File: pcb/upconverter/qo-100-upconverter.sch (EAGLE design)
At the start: 171 parts, among them CON1 2EDG-2P, Q1 AO3400, Q2 AO3401, U1 EFM32PG1B200F256GM32, U10 MIC23155, U11 LT8636, U12 ADP3334, U13 LT8636, U14 ADP150UJZ-3.3, U15 ADP150UJZ-3.3, U2 DSB321SDA, U3 ADF4351, U4 F1951NBGI, U5 MAX2671, U6 2450BP15E0100, U7 ADL5601, U8 ADL5601, U9 ADPA9002

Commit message: Start upconverter redesign
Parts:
- removed C82: 10pF, Capacitor:CAPACITOR-0603
- removed C83, C84, C86, C87: 1uF, Capacitor:CAPACITOR-0603
- removed C85, C88: 22uF, Capacitor:CAPACITOR-1206
- removed C89: 100nF, Capacitor:CAPACITOR-0603
- removed C90: 10uF, Capacitor:CAPACITOR-1206
- removed L11: 47nH, Inductor:INDUCTOR-0603
- removed L12: 2.2uH, Inductor:INDUCTOR-2.5X2X1.2MM
- removed L13, L14: 4.7uH, Inductor:INDUCTOR-6X6MM
- removed Q1: AO3400, Alpha Omega:AO3400
- removed Q2: AO3401, Alpha Omega:AO3401
- removed R36: 1M Ohms, Resistor:RESISTOR-0603
- removed R37: 86.6K Ohms, Resistor:RESISTOR-0603
- removed TP1: TESTPOINT-1.27MM, PADs:TESTPOINT-1.27MM
- C11, C13, C15, C17: value 100nF -> 10pF
- C12, C14, C16, C67: value 10pF -> 100nF
- C18: value 10pF -> 0.7pF
- C20: value 0.7pF -> 15pF
- C21: value 15pF -> 39nF
- C22: value 39nF -> 2.7nF
- C23: value 2.7nF -> 1.2nF
- C24: value 1.2nF -> 100nF
- C26, C28: value 10uF -> 100nF
- C27: value 100nF -> 10uF
- C29: value 100nF -> 100pF
- C30: value 100pF -> 47pF
- C32: value 47pF -> 220pF
- C33: value 220pF -> 15pF
- C34, C49: value DNP -> 100uF; device Capacitor:CAPACITOR-0603 -> Capacitor:CAPACITOR-1206
- C35, C39, C50: value 15pF -> 1uF
- C36: value 100uF -> 1nF; device Capacitor:CAPACITOR-1206 -> Capacitor:CAPACITOR-0603
- C37, C41: value 1uF -> 15pF
- C38, C42: value 1nF -> 15pF
- C4: value 4.7uF -> 1uF
- C40: value 15pF -> 1nF
- C43: value 15pF -> 100nF
- C45: value 0 Ohms -> 10uF
- C46: value 12pF -> 10nF
- C47: value 22uF -> 100pF; device Capacitor:CAPACITOR-1206 -> Capacitor:CAPACITOR-0603; VOLTAGE 25V -> (none)
- C48: value 1nF -> 2pF
- C5, C72: value 1uF -> 100nF
- C51: value DNP -> 3.3F
- C52: value DNP -> 100nF
- C53: value DNP -> 10nF
- C54: value 1nF -> 100pF
- C55: value 100nF -> 15pF
- C56: value 4.7uF -> 15pF; VOLTAGE 35V -> (none)
- C57: VOLTAGE (none) -> 35V
- C58: value 470pF -> 100nF
- C60: value 470pF -> 4.7uF
- C61: value 1uF -> 470pF; VOLTAGE 50V -> (none)
- C62: VOLTAGE (none) -> 50V
- C63, C80: value 10nF -> 470pF
- C64, C78: value 470pF -> 1uF
- C65: value 100nF -> 10nF
- C66: value 100nF -> 470pF
- C68: value 470pF -> 10pF
- C69: value 100uF -> 100nF; device Capacitor:CAPACITOR-1206 -> Capacitor:CAPACITOR-0603
- C71: value 100nF -> 100uF; device Capacitor:CAPACITOR-0603 -> Capacitor:CAPACITOR-1206
- C73: value 4.7uF -> 1uF; VOLTAGE 35V -> (none)
- C74: value 22uF -> 470pF; device Capacitor:CAPACITOR-1206 -> Capacitor:CAPACITOR-0603; VOLTAGE 25V -> (none)
- C75, C77: VOLTAGE 50V -> (none)
- C76: value 100nF -> 1uF
- C81: value 100nF -> 10uF; device Capacitor:CAPACITOR-0603 -> Capacitor:CAPACITOR-1206; VOLTAGE (none) -> 50V
- L1: value 4.7uH -> 3.3nH; OCLCSC C281111 -> (none)
- L10: value 470nH -> 4.7uH; device Inductor:INDUCTOR-0603 -> Inductor:INDUCTOR-6X6MM; CURRENT (none) -> 3A; OCLCSC (none) -> C326336
- L2: value 3.3nH -> 10nH
- L3: value 10nH -> 3.3nH
- L5: value 3.3nH -> 1.8nH
- L6: value 1.8nH -> 470nH
- L7: value DNP -> 470nH
- L8: value DNP -> 47nH
- L9: value 470nH -> 2.2uH; device Inductor:INDUCTOR-0603 -> Inductor:INDUCTOR-2.5X2X1.2MM; CURRENT (none) -> 2.2A; OCLCSC (none) -> C375952
- R10: value 100K Ohms -> 61.9 Ohms
- R11: value 100 Ohms -> 680 Ohms
- R12: value 100K Ohms -> 105 Ohms
- R13: value 510 Ohms -> 100K Ohms
- R14: value 2K Ohms -> 100 Ohms
- R15, R17: value 147K Ohms -> 100K Ohms
- R16: value 21K Ohms -> 510 Ohms
- R18: value 21K Ohms -> 100 Ohms
- R19: value 41.2K Ohms -> 510 Ohms
- R20: value 309K Ohms -> 147K Ohms
- R21: value 71.5K Ohms -> 21K Ohms
- R22: value 100K Ohms -> 41.2K Ohms
- R24: value 1M Ohms -> 100K Ohms
- R25: value 226K Ohms -> 309K Ohms
- R26: value 22 Ohms -> 71.5K Ohms
- R27: value 510 Ohms -> 1M Ohms
- R28: value 10K Ohms -> 226K Ohms
- R29: value 10K Ohms -> 510 Ohms
- R30: value 3.9K Ohms -> 100K Ohms
- R31: value 100K Ohms -> 210K Ohms
- R32: value 210K Ohms -> 64.9K Ohms
- R33: value 64.9K Ohms -> 100K Ohms
- R34: value 41.2K Ohms -> 210K Ohms
- R35: value 100K Ohms -> 64.9K Ohms
- R8: value 360 Ohms -> 105 Ohms
- R9: value 680 Ohms -> 360 Ohms
- U1: value EFM32PG1B200F256GM32 -> EFM32PG1B100F256GM32; device EFM32:EFM32PG1B200F256GM32 -> EFM32:EFM32PG1B100F256GM32
- U13: value LT8636 -> ADP7142AUJZ-3.3; device Analog Devices:LT8636 -> Analog Devices:ADP7142AUJZ-3.3
- U14: value ADP150UJZ-3.3 -> ADP7142AUJZ-3.3; device Analog Devices:ADP150UJZ-3.3 -> Analog Devices:ADP7142AUJZ-3.3
- U15: value ADP150UJZ-3.3 -> ADP3334; device Analog Devices:ADP150UJZ-3.3 -> Analog Devices:ADP3334
- U2: value DSB321SDA -> ADF4351; device Crystal:DSB321SDA -> Analog Devices:ADF4351
- U3: value ADF4351 -> F1951NBGI; device Analog Devices:ADF4351 -> Renesas:F1951NBGI
- U4: value F1951NBGI -> MAX2671; device Renesas:F1951NBGI -> Maxim Integrated:MAX2671
- U5: value MAX2671 -> 2450BP15E0100; device Maxim Integrated:MAX2671 -> Generic Filter:2450BP15E0100
- U6: value 2450BP15E0100 -> ADL5601; device Generic Filter:2450BP15E0100 -> Analog Devices:ADL5601
- U8: value ADL5601 -> F1951NBGI; device Analog Devices:ADL5601 -> Renesas:F1951NBGI
- U9: value ADPA9002 -> ADL5606; device Analog Devices:ADPA9002 -> Analog Devices:ADL5606
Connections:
- removed net !5V0_PA_BIAS_EN: R31.1, U1.PA0, U12.SD
- removed net !ATT_CS: R10.2, U1.PB15, U4.!CS
- removed net 12V0: C82.C1, C85.C1, C88.C1, C89.C1, L14.2, Q2.S, R17.2, R29.2, R36.2, U13.BIAS
- removed net 12V0_ANA_PA_CLEAN: C46.C1, C47.C1, C74.C1, C76.C1, L11.2, Q2.D, R14.2
- removed net 12V0_BST: C81.C2, U13.BST
- removed net 12V0_FB: C82.C2, R36.1, R37.2, U13.FB
- removed net 12V0_INTVCC: C79.C1, U13.INTVCC, U13.SYNC/MODE
- removed net 12V0_PA_BIAS_EN: R26.2, U1.PA1
- removed net 12V0_PGOOD: R35.1, U1.PB14, U13.PG
- removed net 12V0_RT: R34.2, U13.RT
- removed net 12V0_SS: C80.C1, U13.TR/SS
- removed net 12V0_SW: C81.C1, L14.1, U13.SW
- removed net 12V0_VSENSE: C64.C1, R17.1, R18.2, U1.PB12
- removed net 1V8: C4.C1, L1.1, U1.DVDD
- removed net 3V3_ANA_MIXER_CLEAN: C26.C1, C28.C1, C29.C1, C31.C1, C32.C1, C86.C1, L6.2, U14.OUT, U4.VDD, U5.VCC
- removed net 5V0_ANA_PA_CLEAN: C36.C1, C37.C1, C38.C1, C39.C1, C41.C1, C42.C1, C43.C1, C78.C1, L10.2, L9.2, R13.2, R32.2, U12.OUT
- removed net N$11: C45.C1, TP1.TP, U9.VGG
- removed net N$13: C50.C1, L11.1, U9.RFOUT
- removed net N$17: C44.C2, U9.RFIN
- removed net N$21: L1.2, U1.VREGSW
- removed net N$24: D3.A, R14.1
- new net !IF_ATT_CS: U1.PB15, U3.!CS
- new net !IF_ATT_RST: R13.2, U3.!RST
- new net !PA_BIAS_EN: R30.1, R33.1, U1.PA0, U12.SD, U15.SD
- new net !RF_ATT_CS: U8.!CS
- new net !RF_ATT_RST: R17.2, U8.!RST
- new net 3V3_ANA_MIXER_ATT_CLEAN: C25.C1, C27.C1, C28.C1, C30.C1, C31.C1, C43.C1, C78.C1, L5.2, U13.SENSE/ADJ, U13.VOUT, U3.VDD, U4.VCC, U8.VDD
- new net 5V0_PA_STG1_CLEAN: C34.C1, C35.C1, C36.C1, C37.C1, C39.C1, C40.C1, C41.C1, C74.C1, L6.2, L7.2, R16.2, R31.2, U12.OUT
- new net 5V0_PA_STG2_CLEAN: C45.C1, C46.C1, C47.C1, C49.C1, C50.C1, C53.C1, C54.C1, C55.C1, C80.C1, L8.2, R19.2, R34.2, U15.OUT, U9.VBIAS, U9.VCC
- new net N$29: C20.C2, R10.2, R8.2
- new net PA_DISABLE: R18.1
- new net RF_ACC_PRE: C42.C2, U8.RF2
- net !MIXER_SHDN: now also R14.2; no longer R11.2
- net !PLL_MUTE: now also U2.!PDRF; no longer U3.!PDRF
- net 3V3: now also C10.C1, C70.C1, L9.2, R25.2, R30.2, R33.2, U1.DVDD, U2.DVDD; no longer C11.C1, C65.C1, L12.2, R20.2, R31.2, R35.2, U1.VREGVDD, U3.DVDD
- net 3V3_ANA_PLL_CLEAN: now also C6.C1, C79.C1, L1.1, L2.2, U14.SENSE/ADJ, U14.VOUT, U2.AVDD, U2.SDVDD, U2.VP, U2.VVCO@0, U2.VVCO@1; no longer C10.C1, C87.C1, L2.1, L3.2, U15.OUT, U2.VDD, U3.AVDD, U3.SDVDD, U3.VP, U3.VVCO@0, U3.VVCO@1
- net 3V3_FB: now also R25.1, R26.2; no longer R20.1, R21.2
- net 3V3_SOFTSTART: now also C63.C1; no longer C60.C1
- net 3V3_SW: now also L9.1; no longer L12.1
- net 5V0: now also C58.C1, C60.C1, C68.C1, C73.C1, C75.C1, C76.C1, C77.C1, L10.2, R23.2, R29.2, U13.EN, U13.VIN, U15.IN; no longer C55.C1, C57.C1, C67.C1, C70.C1, C83.C1, C84.C1, L13.2, R22.2, R24.2, U15.EN, U15.VIN
- net 5V0_BST: now also C67.C2; no longer C66.C2
- net 5V0_FB: now also C68.C2, R27.1, R28.2; no longer C67.C2, R24.1, R25.2
- net 5V0_INTVCC: now also C64.C1; no longer C62.C1
- net 5V0_RT: now also R22.2; no longer R19.2
- net 5V0_SS: now also C65.C1; no longer C63.C1
- net 5V0_SW: now also C67.C1, L10.1; no longer C66.C1, L13.1
- net 5V0_VSENSE: now also C66.C1, R23.1, R24.2; no longer C68.C1, R22.1, R23.2
- net GND: now also C12.C2, C19.C2, C22.C2, C25.C2, C27.C2, C35.C2, C40.C2, C50.C2, C66.C2, C78.C2, C81.C2, R13.1, R15.1, R17.1, R22.1, R24.1, R26.1, R32.1, R35.1, R9.1, U2.AGND, U2.AGNDVCO@0, U2.AGNDVCO@1, U2.AGNDVCO@2, U2.CPGND, U2.DGND, U2.SDGND, U6.GND@0, U6.GND@1, U8.GND; no longer C11.C2, C18.C2, C20.C2, C24.C2, C26.C2, C32.C2, C38.C2, C42.C2, C56.C2, C68.C2, C74.C2, C80.C2, C83.C2, C84.C2, C85.C2, C86.C2, C87.C2, C88.C2, C89.C2, C90.C2, L7.2, L8.2, Q1.S, R10.1, R16.1, R18.1, R19.1, R23.1, R25.1, R33.1, R34.1, R37.1, U1.VREGVSS, U3.AGND, U3.AGNDVCO@0, U3.AGNDVCO@1, U3.AGNDVCO@2, U3.CPGND, U3.DGND, U3.SDGND, U6.GND, U8.GND@0, U8.GND@1
- net IF_FREQ_SEL: now also C5.C1; no longer C6.C1
- net IF_IN_DCC: now also C24.C1; no longer C25.C1
- net MIXER_LO: now also R10.1, R12.2, U4.LO; no longer C21.C2, U5.LO
- net N$1: now also C18.C2, C20.C1, L3.1; no longer C19.C2, C21.C1, L4.1
- net N$10: now also C52.C1, R18.2, U9.DISABLE; no longer C54.C1, U9.ACG1
- net N$12: now also C33.C2, U6.RFIN; no longer C35.C2, U7.RFIN
- net N$14: now also C38.C1, L6.1, U6.RFOUT; no longer C40.C1, L9.1, U7.RFOUT
- net N$149: now also R29.1; no longer R27.1
- net N$15: now also C38.C2, U7.RFIN; no longer C40.C2, U8.RFIN
- net N$16: now also C42.C1, L7.1, U7.RFOUT; no longer C44.C1, L10.1, U8.RFOUT
- net N$18: now also C56.C2; no longer C50.C2
- net N$2: now also C80.C2, R34.1, R35.2, U15.FB; no longer Q1.G, R26.1, R28.2
- net N$20: now also C74.C2, R31.1, R32.2; no longer C78.C2, R32.1, R33.2
- net N$22: now also C4.C1; no longer C5.C1
- net N$23: now also R16.1; no longer R13.1
- net N$26: now also C24.C2, U3.RF2; no longer C25.C2, U4.RF2
- net N$27: now also C26.C2, U4.IFIN; no longer C27.C2, U5.IFIN
- net N$28: now also C26.C1, U3.RF1; no longer C27.C1, U4.RF1
- net N$3: now also D3.A, R19.1; no longer Q2.G, R29.1, R30.2
- net N$4: now also C29.C1, R14.1, R15.2, U4.!SHDN; no longer C30.C1, R11.1, R12.2, U5.!SHDN
- net N$5: now also C44.C2, C48.C1, U9.RFIN; no longer Q1.D, R30.1
- net N$6: now also C32.C1, L4.2, L5.1; no longer C33.C1, L5.2, L6.1
- net N$67: now also C19.C1, L2.1, L3.2, U2.RFOUTA-; no longer C20.C1, L3.1, L4.2, U3.RFOUTA-
- net N$69: now also C18.C1, L1.2, U2.RFOUTA+; no longer C19.C1, L2.2, U3.RFOUTA+
- net N$7: now also L4.1, U4.RFOUT; no longer L5.1, U5.RFOUT
- net N$8: now also C56.C1, L8.1, U9.RFOUT; no longer C48.C1, C49.C1, U9.ACG3
- net N$84: now also C21.C2, R9.2; no longer C22.C2, R8.2
- net N$88: now also U2.RSET; no longer U3.RSET
- net N$9: now also C44.C1, U8.RF1; no longer C52.C1, C53.C1, U9.ACG2
- net PLL_CP_VOUT: now also C21.C1, R11.2, U2.CPOUT; no longer C23.C1, R9.2, U3.CPOUT
- net PLL_EN: now also U2.CE; no longer U3.CE
- net PLL_FASTLOCK_SW: now also U2.SW; no longer U3.SW
- net PLL_LE: now also U2.LE; no longer U3.LE
- net PLL_LOCK: now also U2.LD; no longer U3.LD
- net PLL_MUXOUT: now also U2.MUXOUT; no longer U3.MUXOUT
- net PLL_REF_ACC: now also C11.C2, U2.REFIN; no longer C12.C2, U3.REFIN
- net PLL_REF_DCC: now also C11.C1; no longer C12.C1, U2.CLK
- net PLL_TEMP: now also C16.C1, U2.TEMP; no longer C18.C1, U3.TEMP
- net PLL_VCOM: now also C14.C1, U2.VCOM; no longer C16.C1, U3.VCOM
- net PLL_VREF: now also C12.C1, U2.VREF; no longer C14.C1, U3.VREF
- net PLL_VTUNE: now also C23.C1, R11.1, U2.VTUNE; no longer C24.C1, R9.1, U3.VTUNE
- net RF_ACC: now also C32.C2, U5.RFIN; no longer C33.C2, C34.C1, L7.1, U6.RFIN
- net RF_ACC_FILT: now also C33.C1, U5.RFOUT; no longer C35.C1, L8.1, U6.RFOUT
- net SPI_MOSI: now also U2.DATA, U3.SDI, U8.SDI; no longer U3.DATA, U4.SDI
- net SPI_SCK: now also U2.CLK, U8.CLK; no longer U4.CLK
- net VIN: now also C57.C1, C62.C1, C81.C1, R20.2; no longer C56.C1, C61.C1, C73.C1, C75.C1, C77.C1, C90.C1, R15.2, U13.EN/UV, U13.VIN
- net VIN_VSENSE: now also C61.C1, R20.1, R21.2; no longer C58.C1, R15.1, R16.2
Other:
- note added: "+20 dB"
- note added: "-9 dB Pi Attenuator"
- note removed: "+13 dB to +15 dB"
- note removed: "Use 68.1K to get higher output power from the last amplifier stage"
- note removed: "VGSon = -8.7V"
- note removed: "Vout = ((R36/R37) + 1) * 0.97"

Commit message: Work on Upconverter
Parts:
- removed JP1: PINHD-1X3, Pin Header:PINHD-1X3
- added C82: 10uF, Capacitor:CAPACITOR-0603
- added C83: 1nF, Capacitor:CAPACITOR-0603
- added C84: 470pF, Capacitor:CAPACITOR-0603
- added C85: 10uF, Capacitor:CAPACITOR-1206
- added CON2: 2EDG-2P-5MM, Generic Connector:2EDG-2P-5MM
- added D6: LED0603, LED:LED0603
- added R36: 210K Ohms, Resistor:RESISTOR-0603
- added R37: 64.9K Ohms, Resistor:RESISTOR-0603
- added R38: 510 Ohms, Resistor:RESISTOR-0603
- added R39: 330 Ohms, Resistor:RESISTOR-0603
- added U16: ADP7142AUJZ-3.3, Analog Devices:ADP7142AUJZ-3.3
- added U17: ADP3334, Analog Devices:ADP3334
- added U18: ADM7171ACPZ-5.0, Analog Devices:ADM7171ACPZ-5.0
- C10, C12, C14, C16, C67: value 100nF -> 10pF
- C11, C13, C15: value 10pF -> 100nF
- C17: value 10pF -> 0.7pF
- C19: value 0.7pF -> 15pF
- C20: value 15pF -> 39nF
- C21: value 39nF -> 2.7nF
- C22: value 2.7nF -> 1.2nF
- C23: value 1.2nF -> 100nF
- C26: value 100nF -> 1uF
- C27: value 10uF -> 100nF
- C28: value 100nF -> 100pF
- C29: value 100pF -> 47pF
- C31: value 47pF -> 220pF
- C32: value 220pF -> 15pF
- C33: value 15pF -> 100uF; device Capacitor:CAPACITOR-0603 -> Capacitor:CAPACITOR-1206
- C34, C49: value 100uF -> 1uF; device Capacitor:CAPACITOR-1206 -> Capacitor:CAPACITOR-0603
- C35, C39: value 1uF -> 1nF
- C36, C40: value 1nF -> 15pF
- C38: value 15pF -> 1uF
- C42, C56: value 15pF -> 100nF
- C43, C52: value 100nF -> 15pF
- C44: value 15pF -> 10uF
- C45: value 10uF -> 10nF
- C46: value 10nF -> 100uF; device Capacitor:CAPACITOR-0603 -> Capacitor:CAPACITOR-1206
- C50, C64: value 1uF -> 10nF
- C51: value 3.3F -> 100pF
- C53: value 10nF -> 3.3F
- C54: value 100pF -> 15pF
- C55: value 15pF -> 4.7uF; VOLTAGE (none) -> 35V
- C57: value 4.7uF -> 470pF; VOLTAGE 35V -> (none)
- C58: value 100nF -> 470pF
- C59: value 1uF -> 4.7uF; VOLTAGE 50V -> (none)
- C60: value 4.7uF -> 1uF; VOLTAGE (none) -> 50V
- C63: value 470pF -> 1uF
- C65: value 10nF -> 100nF
- C66: value 470pF -> 100nF
- C68: value 10pF -> 1uF
- C73: value 1uF -> 100nF
- C74: value 470pF -> 22uF; device Capacitor:CAPACITOR-0603 -> Capacitor:CAPACITOR-1206
- C75: value 1uF -> 15pF
- C80: value 470pF -> 33nF
- C81: device Capacitor:CAPACITOR-1206 -> Capacitor:CAPACITOR-0603; VOLTAGE 50V -> (none)
- CON1: value 2EDG-2P -> 3P-SH-SIDE; device Generic Connector:2EDG-2P -> JST:3P-SH-SIDE
- D4: value LED0603 -> SMAJ24A; device LED:LED0603 -> TVS:SMAJ24A; COLOR GREEN -> (none)
- D5: value SMAJ24A -> LED0603; device TVS:SMAJ24A -> LED:LED0603; COLOR (none) -> GREEN
- R10: value 61.9 Ohms -> DNP
- R11: value 680 Ohms -> 105 Ohms
- R12: value 105 Ohms -> 360 Ohms
- R13: value 100K Ohms -> 61.9 Ohms
- R14: value 100 Ohms -> 680 Ohms
- R15: value 100K Ohms -> 105 Ohms
- R16: value 510 Ohms -> 100K Ohms
- R17, R4, R5: value 100K Ohms -> 100 Ohms
- R18: value 100 Ohms -> 100K Ohms
- R2: value 10K Ohms -> 1K Ohms
- R20: value 147K Ohms -> 100K Ohms
- R21: value 21K Ohms -> 510 Ohms
- R22: value 41.2K Ohms -> 100K Ohms
- R23: value 100K Ohms -> 10K Ohms
- R25: value 309K Ohms -> 100K Ohms
- R26: value 71.5K Ohms -> 41.2K Ohms
- R27: value 1M Ohms -> 309K Ohms
- R28: value 226K Ohms -> 71.5K Ohms
- R29: value 510 Ohms -> 1M Ohms
- R3: value 330 Ohms -> 1K Ohms
- R30: value 100K Ohms -> 226K Ohms
- R31: value 210K Ohms -> 10K Ohms
- R32: value 64.9K Ohms -> 10K Ohms
- R33: value 100K Ohms -> 0.03 Ohms; device Resistor:RESISTOR-0603 -> Resistor:RESISTOR-1206; TOLERANCE (none) -> 1%
- R34: value 210K Ohms -> 100K Ohms
- R35: value 64.9K Ohms -> 100K Ohms
- R6: value 5.1K Ohms -> 330 Ohms
- R7: value DNP -> 100K Ohms
- R8: value 105 Ohms -> 100K Ohms
- R9: value 360 Ohms -> 5.1K Ohms
- U12: value ADP3334 -> MCP3421-A0; device Analog Devices:ADP3334 -> Microchip:MCP3421-A0
- U13: value ADP7142AUJZ-3.3 -> MCP6C02-020; device Analog Devices:ADP7142AUJZ-3.3 -> Microchip:MCP6C02-020
- U14: value ADP7142AUJZ-3.3 -> TX-8010-EAW-1070-25M0000000; device Analog Devices:ADP7142AUJZ-3.3 -> Microchip:TX-8010-EAW-1070-25M0000000
- U15: value ADP3334 -> ADP7142AUJZ-3.3; device Analog Devices:ADP3334 -> Analog Devices:ADP7142AUJZ-3.3
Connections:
- removed net !PA_BIAS_EN: R30.1, R33.1, U1.PA0, U12.SD, U15.SD
- removed net 3V3_ANA_MIXER_ATT_CLEAN: C25.C1, C27.C1, C28.C1, C30.C1, C31.C1, C43.C1, C78.C1, L5.2, U13.SENSE/ADJ, U13.VOUT, U3.VDD, U4.VCC, U8.VDD
- removed net 3V3_ANA_PLL_CLEAN: C6.C1, C7.C1, C79.C1, C8.C1, C9.C1, L1.1, L2.2, U14.SENSE/ADJ, U14.VOUT, U2.AVDD, U2.SDVDD, U2.VP, U2.VVCO@0, U2.VVCO@1
- removed net IF_FREQ_SEL: C5.C1, JP1-2.S, R2.2, U1.PC11
- removed net PA_DISABLE: R18.1
- removed net PLL_REF_DCC: C11.C1
- new net !PA_STG1_BIAS_EN: R35.1, U1.PB12, U17.SD
- new net 3V3_MIXER_CLEAN: C24.C1, C26.C1, C27.C1, C29.C1, C30.C1, C81.C1, L5.2, U15.SENSE/ADJ, U15.VOUT, U3.VDD, U4.VCC
- new net 3V3_PLL_CLEAN: C5.C1, C6.C1, C7.C1, C8.C1, C82.C1, L1.1, L2.2, U14.OE, U14.VDD, U16.SENSE/ADJ, U16.VOUT, U2.AVDD, U2.SDVDD, U2.VP, U2.VVCO@0, U2.VVCO@1
- new net 5V0_ISENSE: C74.C1, C76.C1, C77.C1, C78.C1, C79.C1, R33.1, U13.VIM, U15.EN, U15.VIN, U16.EN, U16.VIN, U17.IN, U18.VIN
- new net 5V0_ISENSE_VN: C72.C2, R32.1, U12.VIN-
- new net 5V0_ISENSE_VP: C72.C1, R31.1, U12.VIN+
- new net I2C_SCL: R2.1, U1.PC7, U12.SCL
- new net I2C_SDA: R3.1, U1.PC8, U12.SDA
- new net N$11: CON1-2.S, R5.1
- new net N$13: D6.A, R39.1
- new net N$17: CON1-1.S, R4.1
- new net N$21: C10.C1, C75.C1, U14.CLK
- new net N$24: C80.C1, U14.FLT
- new net PA_STG2_BIAS_EN: R34.2, U1.PB13, U18.EN
- new net UART_RX: R4.2, U1.PC10
- new net UART_TX: R5.2, U1.PC11
- net !IF_ATT_CS: now also U1.PF3; no longer U1.PB15
- net !IF_ATT_RST: now also R16.2, U1.PF4; no longer R13.2
- net !MIXER_SHDN: now also R17.2, U1.PD9; no longer R14.2, U1.PF3
- net !PLL_MUTE: now also R8.2, U1.PD15; no longer R5.2, U1.PD14
- net !RF_ATT_CS: now also U1.PA0
- net !RF_ATT_RST: now also R20.2, U1.PA1; no longer R17.2
- net 3V3: now also C65.C1, C9.C1, R2.2, R27.2, R3.2, R35.2, U12.VDD; no longer C10.C1, JP1-1.S, R25.2, R30.2, R33.2
- net 3V3_FB: now also R27.1, R28.2; no longer R25.1, R26.2
- net 3V3_SOFTSTART: now also C61.C1; no longer C63.C1
- net 5V0: now also C56.C1, C59.C1, C67.C1, R24.2, R33.2, R38.2, U13.VDD, U13.VIP; no longer C58.C1, C60.C1, C72.C1, C75.C1, C76.C1, C77.C1, R23.2, R27.2, U12.IN, U13.EN, U13.VIN, U14.EN, U14.VIN, U15.IN
- net 5V0_BST: now also C66.C2; no longer C67.C2
- net 5V0_FB: now also C67.C2, R29.1, R30.2; no longer C68.C2, R27.1, R28.2
- net 5V0_INTVCC: now also C63.C1; no longer C64.C1
- net 5V0_PA_STG1_CLEAN: now also C33.C1, C38.C1, C42.C1, C84.C1, R19.2, R36.2, U17.OUT, U8.VDD; no longer C37.C1, C41.C1, C74.C1, R16.2, R31.2, U12.OUT
- net 5V0_PA_STG2_CLEAN: now also C44.C1, C51.C1, C52.C1, R21.2, U18.SENSE, U18.VOUT; no longer C53.C1, C54.C1, C55.C1, C80.C1, R19.2, R34.2, U15.OUT
- net 5V0_RT: now also R26.2; no longer R22.2
- net 5V0_SS: now also C64.C1; no longer C65.C1
- net 5V0_SW: now also C66.C1; no longer C67.C1
- net 5V0_VSENSE: now also C58.C1, R24.1, R25.2, U1.PB14; no longer C66.C1, R23.1, R24.2, U1.PB11
- net GND: now also C11.C2, C18.C2, C21.C2, C24.C2, C26.C2, C33.C2, C38.C2, C42.C2, C44.C2, C56.C2, C68.C2, C74.C2, C80.C2, C82.C2, C83.C2, C85.C2, CON1-3.S, CON2-1.S, D4.A, D5.C, D6.C, R11.1, R16.1, R18.1, R20.1, R23.1, R25.1, R30.1, R32.2, R34.1, R37.1, R7.1, U12.VSS, U13.VREF, U13.VSS, U16.GND, U17.GND, U18.GND, U9.DISABLE; no longer C10.C2, C17.C2, C19.C2, C23.C2, C25.C2, C31.C2, C37.C2, C41.C2, C43.C2, C54.C2, C66.C2, C72.C2, CON1-1.S, D4.C, D5.A, JP1-3.S, R13.1, R17.1, R2.1, R21.1, R22.1, R24.1, R32.1, R35.1, R4.1, R5.1, R6.1, U12.GND, U13.GND
- net IF_IN_DCC: now also C23.C1; no longer C24.C1
- net LED: now also R6.2, U1.PC9; no longer R3.2, U1.PC10
- net MIXER_LO: now also R13.1, R15.2; no longer R10.1, R12.2
- net N$1: now also C17.C2, C19.C1; no longer C18.C2, C20.C1
- net N$10: now also R31.2, U13.VOUT; no longer C52.C1, R18.2, U9.DISABLE
- net N$12: now also C32.C2; no longer C33.C2
- net N$14: now also C37.C1; no longer C38.C1
- net N$149: now also D5.A, R38.1; no longer D4.A, R29.1
- net N$15: now also C37.C2; no longer C38.C2
- net N$16: now also C41.C1; no longer C42.C1
- net N$18: now also C54.C2; no longer C56.C2
- net N$19: now also CON2-2.S; no longer CON1-2.S
- net N$2: now also C83.C1, U18.SS; no longer C80.C2, R34.1, R35.2, U15.FB
- net N$20: now also C84.C2, R36.1, R37.2, U17.FB; no longer C74.C2, R31.1, R32.2, U12.FB
- net N$23: now also R19.1; no longer R16.1
- net N$25: now also R6.1; no longer R3.1
- net N$26: now also C23.C2; no longer C24.C2
- net N$27: now also C25.C2; no longer C26.C2
- net N$28: now also C25.C1; no longer C26.C1
- net N$29: now also C19.C2, R11.2, R13.2; no longer C20.C2, R10.2, R8.2
- net N$3: now also R21.1; no longer R19.1
- net N$4: now also C28.C1, R17.1, R18.2; no longer C29.C1, R14.1, R15.2
- net N$5: now also C43.C2; no longer C44.C2
- net N$6: now also C31.C1; no longer C32.C1
- net N$67: now also C18.C1; no longer C19.C1
- net N$69: now also C17.C1; no longer C18.C1
- net N$8: now also C53.C1, C54.C1; no longer C51.C1, C56.C1
- net N$84: now also C20.C2, R10.1, R12.2; no longer C21.C2, R7.1, R9.2
- net N$88: now also R9.2; no longer R6.2
- net N$9: now also C43.C1; no longer C44.C1
- net PLL_CP_VOUT: now also C20.C1, R14.2; no longer C22.C1, R11.2
- net PLL_EN: now also R7.2, U1.PD10; no longer R4.2, U1.PD9
- net PLL_FASTLOCK_SW: now also R10.2; no longer R7.2
- net PLL_LE: now also U1.PD11; no longer U1.PD10
- net PLL_LOCK: now also R39.2; no longer U1.PD15
- net PLL_MUXOUT: now also U1.PD14; no longer U1.PD13
- net PLL_REF_ACC: now also C10.C2; no longer C11.C2
- net PLL_TEMP: now also C15.C1; no longer C17.C1
- net PLL_VCOM: now also C13.C1; no longer C15.C1
- net PLL_VREF: now also C11.C1; no longer C13.C1
- net PLL_VTUNE: now also C22.C1, R14.1; no longer C23.C1, R11.1
- net RF_ACC: now also C31.C2; no longer C32.C2
- net RF_ACC_FILT: now also C32.C1; no longer C33.C1
- net RF_ACC_PRE: now also C41.C2; no longer C42.C2
- net SPI_MOSI: now also U1.PD12; no longer U1.PD11
- net SPI_SCK: now also U1.PD13; no longer U1.PD12
- net VIN: now also C55.C1, C60.C1, C85.C1, D4.C, R22.2; no longer C57.C1, C59.C1, C81.C1, D5.C, R20.2
- net VIN_VSENSE: now also C57.C1, R22.1, R23.2, U1.PB15; no longer C61.C1, R20.1, R21.2, U1.PB13
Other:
- note added: "Kelvin connection to R33"
- note removed: "IF Frequency selector 0 = 433 MHz (default) 1 = 144 MHz"
- moved on the sheet: C10, C11, C12, C13, C14, C15, C16, C17, C18, C19, C20, C21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

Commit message: Change Upconverter pre-amplifier
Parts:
- removed U18: ADM7171ACPZ-5.0, Analog Devices:ADM7171ACPZ-5.0
- added C86: 10uF, Capacitor:CAPACITOR-1206
- added L11: 4.7uH, Inductor:INDUCTOR-6X6MM
- added R40: 64.9K Ohms, Resistor:RESISTOR-0603
- added R41: 510 Ohms, Resistor:RESISTOR-0603
- added RFCON3: RFCON-SMA-EDGE, RF Connector:RFCON-SMA-EDGE
- C10: value 10pF -> 100nF
- C17: value 0.7pF -> 100nF
- C18: value 0.7pF -> 10pF
- C19: value 15pF -> 0.7pF
- C20: value 39nF -> 0.7pF
- C21: value 2.7nF -> 15pF
- C22: value 1.2nF -> 39nF
- C23: value 100nF -> 2.7nF
- C24: value 100nF -> 1.2nF
- C26, C68, C76: value 1uF -> 100nF
- C28: value 100pF -> 1uF
- C29: value 47pF -> 100nF
- C30: value 47pF -> 100pF
- C31: value 220pF -> 47pF
- C32: value 15pF -> 47pF
- C33: value 100uF -> 220pF; device Capacitor:CAPACITOR-1206 -> Capacitor:CAPACITOR-0603
- C34, C49: value 1uF -> 100uF; device Capacitor:CAPACITOR-0603 -> Capacitor:CAPACITOR-1206
- C35: value 1nF -> 1uF
- C36, C41: value 15pF -> 1nF
- C37: value 15pF -> 0.5pF
- C38: value 1uF -> 15pF
- C39: value 1nF -> 100nF
- C40, C52: value 15pF -> 1uF
- C42, C9: value 100nF -> 15pF
- C43: value 15pF -> 10pF
- C44: value 10uF -> 1.2pF
- C45: value 10nF -> 100nF
- C46: value 100uF -> 15pF; device Capacitor:CAPACITOR-1206 -> Capacitor:CAPACITOR-0603
- C47: value 100pF -> 10uF
- C48: value 2pF -> 10nF
- C50: value 10nF -> 100pF
- C51: value 100pF -> 2pF
- C53: value 3.3F -> 10nF
- C54: value 15pF -> 100pF
- C55: value 4.7uF -> 15pF; VOLTAGE 35V -> (none)
- C56: value 100nF -> 3.3F
- C57: value 470pF -> 15pF
- C58: value 470pF -> 4.7uF; VOLTAGE (none) -> 35V
- C59: value 4.7uF -> 100nF
- C60: value 1uF -> 470pF; VOLTAGE 50V -> (none)
- C62: value 1uF -> 4.7uF; VOLTAGE 50V -> (none)
- C63: VOLTAGE (none) -> 50V
- C64: value 10nF -> 470pF
- C65: value 100nF -> 1uF; VOLTAGE (none) -> 50V
- C66: value 100nF -> 1uF
- C67: value 10pF -> 10nF
- C7: value 100nF -> 33nF
- C70: value 100uF -> 10pF; device Capacitor:CAPACITOR-1206 -> Capacitor:CAPACITOR-0603
- C71: value 100uF -> 1uF; device Capacitor:CAPACITOR-1206 -> Capacitor:CAPACITOR-0603
- C73: value 100nF -> 100uF; device Capacitor:CAPACITOR-0603 -> Capacitor:CAPACITOR-1206
- C74: value 22uF -> 100uF
- C75: value 15pF -> 100nF
- C77: value 1uF -> 22uF; device Capacitor:CAPACITOR-0603 -> Capacitor:CAPACITOR-1206
- C80: value 33nF -> 1uF
- C81: value 10uF -> 1uF
- C83: value 1nF -> 10uF
- C84: value 470pF -> 1nF
- C85: value 10uF -> 470pF; device Capacitor:CAPACITOR-1206 -> Capacitor:CAPACITOR-0603; VOLTAGE 50V -> (none)
- D2: COLOR RED -> BLUE
- D4: value SMAJ24A -> LED0603; device TVS:SMAJ24A -> LED:LED0603; COLOR (none) -> RED
- D5: value LED0603 -> SMAJ24A; device LED:LED0603 -> TVS:SMAJ24A; COLOR GREEN -> (none)
- D6: COLOR BLUE -> GREEN
- L10: value 4.7uH -> 2.2uH; device Inductor:INDUCTOR-6X6MM -> Inductor:INDUCTOR-2.5X2X1.2MM; CURRENT 3A -> 2.2A; OCLCSC C326336 -> C375952
- L6: value 470nH -> 3.9nH
- L7: value 470nH -> 3nH
- L8: value 47nH -> 62nH
- L9: value 2.2uH -> 62nH; device Inductor:INDUCTOR-2.5X2X1.2MM -> Inductor:INDUCTOR-0603; CURRENT 2.2A -> (none); OCLCSC C375952 -> (none)
- R10: value DNP -> 5.1K Ohms
- R11: value 105 Ohms -> DNP
- R12: value 360 Ohms -> 105 Ohms
- R13: value 61.9 Ohms -> 360 Ohms
- R14: value 680 Ohms -> 61.9 Ohms
- R15: value 105 Ohms -> 680 Ohms
- R16: value 100K Ohms -> 105 Ohms
- R17: value 100 Ohms -> 100K Ohms
- R18: value 100K Ohms -> 100 Ohms
- R19, R38: value 510 Ohms -> 100K Ohms
- R20: value 100K Ohms -> 0 Ohms; device Resistor:RESISTOR-0603 -> Resistor:RESISTOR-SEL-0603
- R21: value 510 Ohms -> 10K Ohms
- R22, R24: value 100K Ohms -> 510 Ohms
- R23: value 10K Ohms -> 100K Ohms
- R26: value 41.2K Ohms -> 10K Ohms
- R27: value 309K Ohms -> 100K Ohms
- R28: value 71.5K Ohms -> 100K Ohms
- R29: value 1M Ohms -> 41.2K Ohms
- R30: value 226K Ohms -> 309K Ohms
- R31: value 10K Ohms -> 71.5K Ohms
- R32: value 10K Ohms -> 1M Ohms
- R33: value 0.03 Ohms -> 226K Ohms; device Resistor:RESISTOR-1206 -> Resistor:RESISTOR-0603; TOLERANCE 1% -> (none)
- R34, R35: value 100K Ohms -> 10K Ohms
- R36: value 210K Ohms -> 0.03 Ohms; device Resistor:RESISTOR-0603 -> Resistor:RESISTOR-1206; TOLERANCE (none) -> 1%
- R37: value 64.9K Ohms -> 100K Ohms
- R39: value 330 Ohms -> 210K Ohms
- R9: value 5.1K Ohms -> 330 Ohms
- RFCON2: value RFCON-SMA-EDGE -> RFCON-U.FL; device RF Connector:RFCON-SMA-EDGE -> RF Connector:RFCON-U.FL
- U14: value TX-8010-EAW-1070-25M0000000 -> ADP7142AUJZ-3.3; device Microchip:TX-8010-EAW-1070-25M0000000 -> Analog Devices:ADP7142AUJZ-3.3
- U16: value ADP7142AUJZ-3.3 -> ADP3334; device Analog Devices:ADP7142AUJZ-3.3 -> Analog Devices:ADP3334
- U17: value ADP3334 -> ADM7171ACPZ-5.0; device Analog Devices:ADP3334 -> Analog Devices:ADM7171ACPZ-5.0
- U2: value ADF4351 -> TX-8010-EAW-1070-25M0000000; device Analog Devices:ADF4351 -> Microchip:TX-8010-EAW-1070-25M0000000
- U3: value F1951NBGI -> ADF4351; device Renesas:F1951NBGI -> Analog Devices:ADF4351
- U4: value MAX2671 -> F1951NBGI; device Maxim Integrated:MAX2671 -> Renesas:F1951NBGI
- U5: value 2450BP15E0100 -> MAX2671; device Generic Filter:2450BP15E0100 -> Maxim Integrated:MAX2671
- U6: value ADL5601 -> 2450BP15E0100; device Analog Devices:ADL5601 -> Generic Filter:2450BP15E0100
- U7: value ADL5601 -> F1478NLGA; device Analog Devices:ADL5601 -> Renesas:F1478NLGA
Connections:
- new net N$30: C39.C2, U7.RFIN
- new net N$31: C33.C2, R20.2
- new net N$32: R20.COM, RFCON2.SIGNAL
- net !IF_ATT_CS: now also U4.!CS; no longer U3.!CS
- net !IF_ATT_RST: now also R17.2, U4.!RST; no longer R16.2, U3.!RST
- net !MIXER_SHDN: now also R18.2; no longer R17.2
- net !PA_STG1_BIAS_EN: now also R38.1, U16.SD; no longer R35.1, U17.SD
- net !PLL_MUTE: now also U3.!PDRF; no longer U2.!PDRF
- net !RF_ATT_RST: now also R23.2; no longer R20.2
- net 3V3: now also C11.C1, C68.C1, C72.C1, C73.C1, L10.2, R30.2, R38.2, U3.DVDD; no longer C65.C1, C69.C1, C70.C1, C9.C1, L9.2, R27.2, R35.2, U2.DVDD
- net 3V3_FB: now also R30.1, R31.2; no longer R27.1, R28.2
- net 3V3_MIXER_CLEAN: now also C28.C1, C31.C1, C32.C1, C82.C1, U14.SENSE/ADJ, U14.VOUT, U4.VDD, U5.VCC; no longer C24.C1, C27.C1, C30.C1, C81.C1, U15.SENSE/ADJ, U15.VOUT, U3.VDD, U4.VCC
- net 3V3_PLL_CLEAN: now also C10.C1, C83.C1, U15.SENSE/ADJ, U15.VOUT, U2.OE, U2.VDD, U3.AVDD, U3.SDVDD, U3.VP, U3.VVCO@0, U3.VVCO@1; no longer C7.C1, C82.C1, U14.OE, U14.VDD, U16.SENSE/ADJ, U16.VOUT, U2.AVDD, U2.SDVDD, U2.VP, U2.VVCO@0, U2.VVCO@1
- net 3V3_SOFTSTART: now also C64.C1; no longer C61.C1
- net 3V3_SW: now also L10.1; no longer L9.1
- net 5V0: now also C62.C1, C70.C1, C74.C1, C76.C1, L11.2, R27.2, R32.2, R36.2, R41.2; no longer C56.C1, C67.C1, C68.C1, C73.C1, L10.2, R24.2, R29.2, R33.2, R38.2
- net 5V0_BST: now also C69.C2; no longer C66.C2
- net 5V0_FB: now also C70.C2, R32.1, R33.2; no longer C67.C2, R29.1, R30.2
- net 5V0_INTVCC: now also C66.C1; no longer C63.C1
- net 5V0_ISENSE: now also C80.C1, C81.C1, R36.1, U14.EN, U14.VIN, U16.IN, U17.VIN; no longer C74.C1, C76.C1, R33.1, U16.EN, U16.VIN, U17.IN, U18.VIN
- net 5V0_ISENSE_VN: now also C75.C2, R35.1; no longer C72.C2, R32.1
- net 5V0_ISENSE_VP: now also C75.C1, R34.1; no longer C72.C1, R31.1
- net 5V0_PA_STG1_CLEAN: now also C41.C1, C45.C1, C85.C1, L8.2, R22.2, R39.2, U16.OUT, U7.BIAS1; no longer C33.C1, C39.C1, C84.C1, L6.2, R19.2, R36.2, U17.OUT
- net 5V0_PA_STG2_CLEAN: now also C48.C1, C53.C1, C54.C1, C55.C1, L9.2, R24.2, U17.SENSE, U17.VOUT; no longer C44.C1, C45.C1, C46.C1, C51.C1, L8.2, R21.2, U18.SENSE, U18.VOUT
- net 5V0_RT: now also R29.2; no longer R26.2
- net 5V0_SS: now also C67.C1; no longer C64.C1
- net 5V0_SW: now also C69.C1, L11.1; no longer C66.C1, L10.1
- net 5V0_VSENSE: now also C61.C1, R27.1, R28.2; no longer C58.C1, R24.1, R25.2
- net GND: now also C10.C2, C17.C2, C20.C2, C23.C2, C31.C2, C32.C2, C37.C2, C41.C2, C54.C2, C66.C2, C67.C2, C72.C2, C84.C2, C86.C2, D4.C, D5.A, L6.1, R10.1, R13.1, R17.1, R19.1, R21.1, R29.1, R31.1, R33.1, R35.2, R40.1, RFCON3.GND, U3.AGND, U3.AGNDVCO@0, U3.AGNDVCO@1, U3.AGNDVCO@2, U3.CPGND, U3.DGND, U3.SDGND, U6.GND, U7.GND; no longer C12.C2, C21.C2, C22.C2, C27.C2, C33.C2, C39.C2, C46.C2, C57.C2, C69.C2, C70.C2, C75.C2, C85.C2, D4.A, D5.C, R11.1, R15.1, R18.1, R20.1, R25.1, R30.1, R32.2, R34.1, R9.1, U18.GND, U2.AGND, U2.AGNDVCO@0, U2.AGNDVCO@1, U2.AGNDVCO@2, U2.CPGND, U2.DGND, U2.SDGND, U6.GND@0, U6.GND@1, U7.GND@0, U7.GND@1
- net IF_IN_DCC: now also C25.C1; no longer C23.C1
- net MIXER_LO: now also R14.1, R16.2, U5.LO; no longer R13.1, R15.2, U4.LO
- net N$1: now also C19.C2, C21.C1; no longer C17.C2, C19.C1
- net N$10: now also R34.2; no longer R31.2
- net N$12: now also L7.1, U7.VCC; no longer C32.C2, U6.RFIN
- net N$13: now also D2.A, R9.1; no longer D6.A, R39.1
- net N$14: now also C43.C1, L8.1, U7.RFOUT; no longer C37.C1, L6.1, U6.RFOUT
- net N$149: now also D6.A, R41.1; no longer D5.A, R38.1
- net N$15: now also R21.2, U7.RSET; no longer C37.C2, U7.RFIN
- net N$16: now also L6.2, U7.BIAS2; no longer C41.C1, L7.1, U7.RFOUT
- net N$18: now also C57.C2, RFCON3.SIGNAL; no longer C54.C2, RFCON2.SIGNAL
- net N$2: now also C84.C1, U17.SS; no longer C83.C1, U18.SS
- net N$20: now also C85.C2, R39.1, R40.2, U16.FB; no longer C84.C2, R36.1, R37.2, U17.FB
- net N$21: now also C12.C1, C9.C1, U2.CLK; no longer C10.C1, C75.C1, U14.CLK
- net N$23: now also D3.A, R22.1; no longer D2.A, R19.1
- net N$24: now also C7.C1, U2.FLT; no longer C80.C1, U14.FLT
- net N$26: now also C25.C2, U4.RF2; no longer C23.C2, U3.RF2
- net N$27: now also C27.C2, U5.IFIN; no longer C25.C2, U4.IFIN
- net N$28: now also C27.C1, U4.RF1; no longer C25.C1, U3.RF1
- net N$29: now also C21.C2, R12.2, R14.2; no longer C19.C2, R11.2, R13.2
- net N$3: now also D4.A, R24.1; no longer D3.A, R21.1
- net N$4: now also C30.C1, R18.1, R19.2, U5.!SHDN; no longer C28.C1, R17.1, R18.2, U4.!SHDN
- net N$5: now also C46.C2, C51.C1; no longer C43.C2, C48.C1
- net N$6: now also C33.C1; no longer C31.C1
- net N$67: now also C20.C1, U3.RFOUTA-; no longer C18.C1, U2.RFOUTA-
- net N$69: now also C19.C1, U3.RFOUTA+; no longer C17.C1, U2.RFOUTA+
- net N$7: now also U5.RFOUT; no longer U4.RFOUT
- net N$8: now also C56.C1, C57.C1, L9.1; no longer C53.C1, C54.C1, L8.1
- net N$84: now also C22.C2, R11.1, R13.2; no longer C20.C2, R10.1, R12.2
- net N$88: now also R10.2, U3.RSET; no longer R9.2, U2.RSET
- net N$9: now also C46.C1; no longer C43.C1
- net PA_STG2_BIAS_EN: now also R37.2, U17.EN; no longer R34.2, U18.EN
- net PLL_CP_VOUT: now also C22.C1, C23.C1, R15.2, U3.CPOUT; no longer C20.C1, C21.C1, R14.2, U2.CPOUT
- net PLL_EN: now also U3.CE; no longer U2.CE
- net PLL_FASTLOCK_SW: now also R11.2, U3.SW; no longer R10.2, U2.SW
- net PLL_LE: now also U3.LE; no longer U2.LE
- net PLL_LOCK: now also R9.2, U3.LD; no longer R39.2, U2.LD
- net PLL_MUXOUT: now also U3.MUXOUT; no longer U2.MUXOUT
- net PLL_REF_ACC: now also C12.C2, U3.REFIN; no longer C10.C2, U2.REFIN
- net PLL_TEMP: now also C17.C1, C18.C1, U3.TEMP; no longer C15.C1, C16.C1, U2.TEMP
- net PLL_VCOM: now also C15.C1, C16.C1, U3.VCOM; no longer C13.C1, C14.C1, U2.VCOM
- net PLL_VREF: now also C13.C1, C14.C1, U3.VREF; no longer C11.C1, C12.C1, U2.VREF
- net PLL_VTUNE: now also C24.C1, R15.1, U3.VTUNE; no longer C22.C1, R14.1, U2.VTUNE
- net RF_ACC: now also R20.1, U6.RFIN; no longer C31.C2, U5.RFIN
- net RF_ACC_FILT: now also C37.C1, C39.C1, U6.RFOUT; no longer C32.C1, U5.RFOUT
- net RF_ACC_PRE: now also C43.C2, C44.C1; no longer C41.C2
- net SPI_MOSI: now also U3.DATA, U4.SDI; no longer U2.DATA, U3.SDI
- net SPI_SCK: now also U4.CLK; no longer U2.CLK
- net VIN: now also C58.C1, C63.C1, C65.C1, C86.C1, D5.C, R25.2; no longer C55.C1, C60.C1, C62.C1, C85.C1, D4.C, R22.2
- net VIN_VSENSE: now also C60.C1, R25.1, R26.2; no longer C57.C1, R22.1, R23.2
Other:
- note added: "+30 dB"
- note removed: "+13.8 dB"
- moved on the sheet: C10, C11, C12, C13, C14, C15, C16, C17, C18, C19, C20, C21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

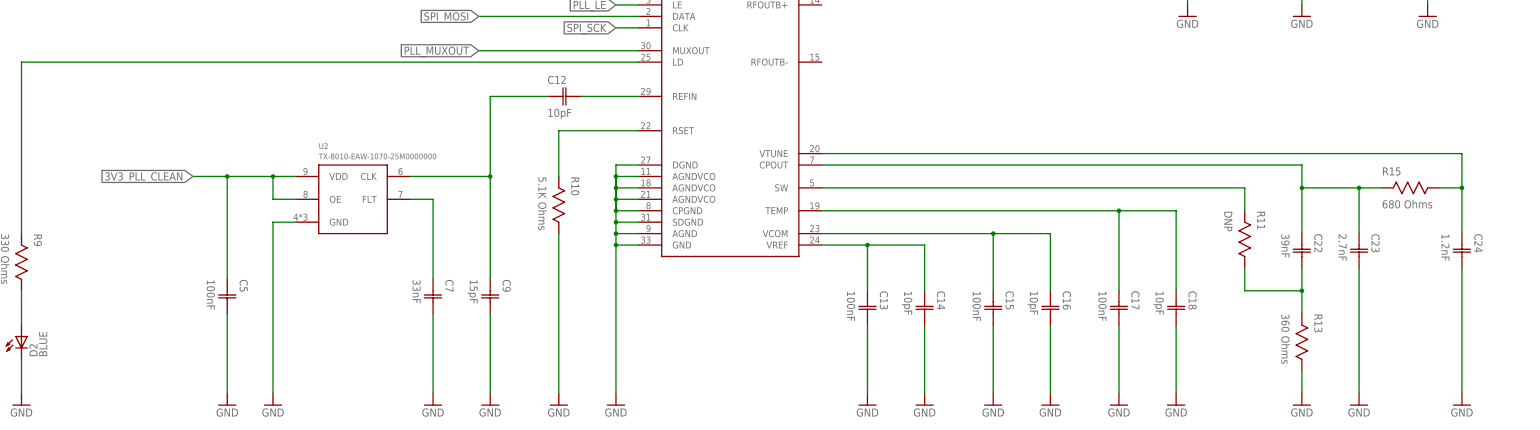
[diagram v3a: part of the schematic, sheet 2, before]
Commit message: Nothing to do on Upconverter
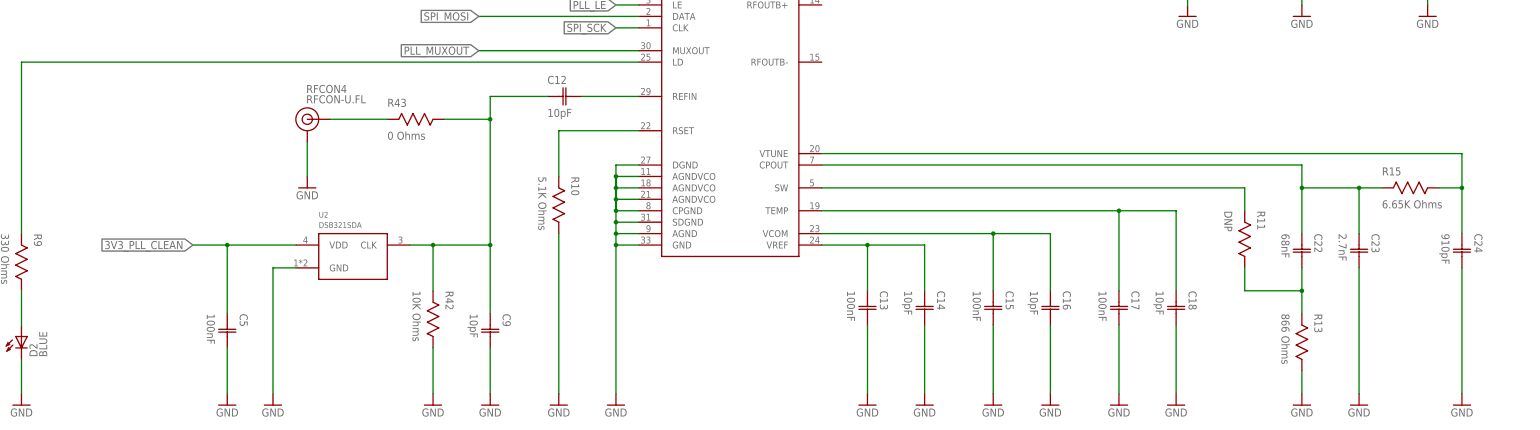
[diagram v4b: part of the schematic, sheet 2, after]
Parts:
- removed C7: 33nF, Capacitor:CAPACITOR-0603
- added R42: 10K Ohms, Resistor:RESISTOR-0603
- added R43: 0 Ohms, Resistor:RESISTOR-0603
- added RFCON4: RFCON-U.FL, RF Connector:RFCON-U.FL
- C22: value 39nF -> 68nF
- C24: value 1.2nF -> 910pF
- C9: value 15pF -> 10pF
- R13: value 360 Ohms -> 866 Ohms
- R15: value 680 Ohms -> 6.65K Ohms
- U2: value TX-8010-EAW-1070-25M0000000 -> DSB321SDA; device Microchip:TX-8010-EAW-1070-25M0000000 -> Crystal:DSB321SDA
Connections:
- removed net N$24: C7.C1, U2.FLT
- new net PLL_REF_DCC: C12.C1, C9.C1, R42.2, R43.1, U2.CLK
- net 3V3_PLL_CLEAN: no longer U2.OE
- net GND: now also R42.1, RFCON4.GND; no longer C7.C2
- net N$21: now also R43.2, RFCON4.SIGNAL; no longer C12.C1, C9.C1, U2.CLK
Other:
- moved on the sheet: C5, C9
